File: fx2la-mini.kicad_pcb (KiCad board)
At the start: 4 copper layers, 21 x 13 mm, 26 parts, among them J1 USB_C_Receptacle_USB2.0, J2 Conn_02x05_Counter_Clockwise, U1 CY7C68013A-56LTX, U2 NUF8401MNT4G, U3 MIC5504-3.3YM5, U4 USBLC6-2SC6, Y1 24 MHz

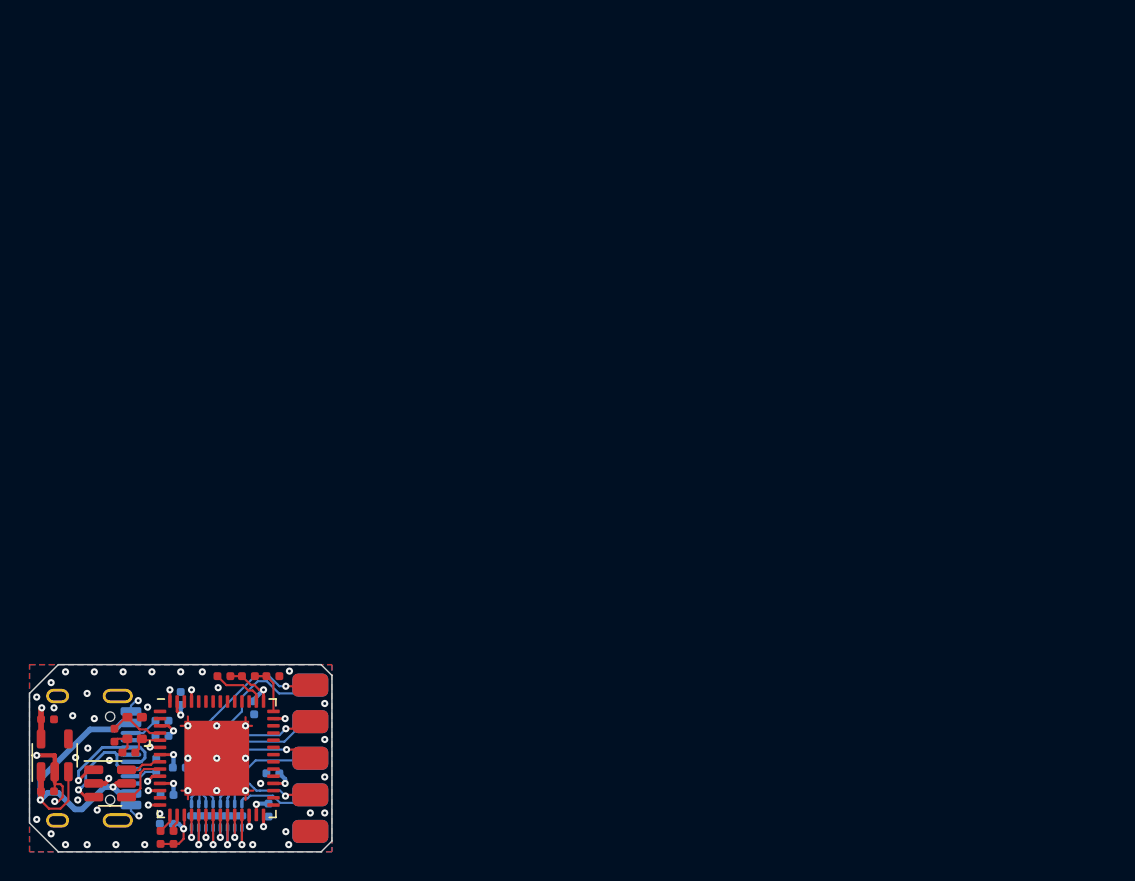
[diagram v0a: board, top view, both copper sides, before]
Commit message: Hijack project to 16 channels
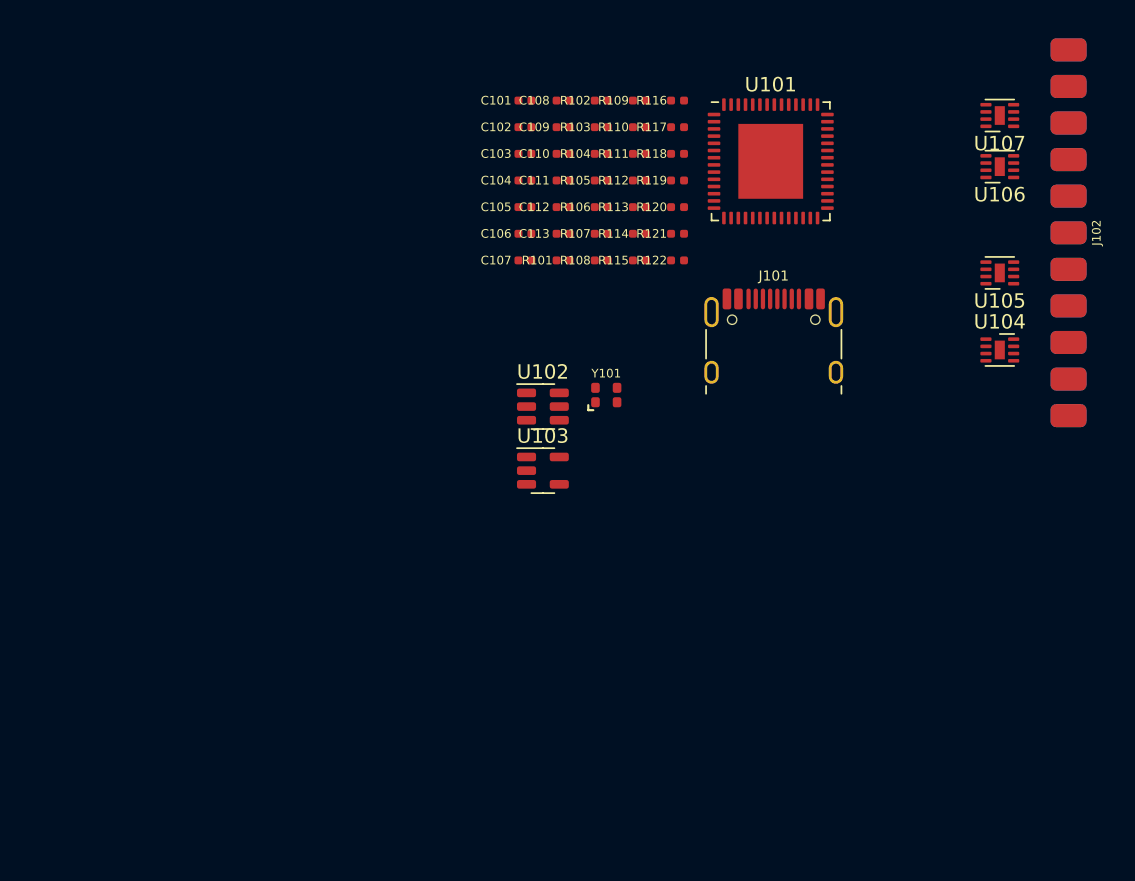
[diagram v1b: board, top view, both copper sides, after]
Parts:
- removed C1, C2: ~, passive:C_0402
- removed C10, C11, C12, C3, C4, C5, C6, C7, C9: 0.1u, passive:C_0402
- removed C13, C8: 4.7u, passive:C_0402
- removed J1: USB_C_Receptacle_USB2.0, connectors:USB_C_Receptacle_USB4105
- removed J2: Conn_02x05_Counter_Clockwise, connectors:2x5_2.54mm_side
- removed R1, R2, R3, R4, R5, R6: 5.1k, passive:R_0402
- removed U1: CY7C68013A-56LTX, Package_DFN_QFN:QFN-56-1EP_8x8mm_P0.5mm_EP4.5x5.2mm
- removed U2: NUF8401MNT4G, dfn:DFN-16-1EP_1.6x4mm_P0.5mm
- removed U3: MIC5504-3.3YM5, Package_TO_SOT_SMD:SOT-23-5
- removed U4: USBLC6-2SC6, Package_TO_SOT_SMD:SOT-23-6
- removed Y1: 24 MHz, crystals:Crystal_4Pin_2.0x1.6mm
- added C101: 16p, passive:C_0402, F.Cu at (146.4, 70.8)
- added C102: 16p, passive:C_0402, F.Cu at (146.4, 72.7)
- added C103: 100n, passive:C_0402, F.Cu at (146.4, 74.5)
- added C104: 100n, passive:C_0402, F.Cu at (146.4, 76.4)
- added C105: 100n, passive:C_0402, F.Cu at (146.4, 78.2)
- added C106: 100n, passive:C_0402, F.Cu at (146.4, 80.1)
- added C107: 100n, passive:C_0402, F.Cu at (146.4, 81.9)
- added C108: 4.7u, passive:C_0402, F.Cu at (149.1, 70.8)
- added C109: 100n, passive:C_0402, F.Cu at (149.1, 72.7)
- added C110: 100n, passive:C_0402, F.Cu at (149.1, 74.5)
- added C111: 100n, passive:C_0402, F.Cu at (149.1, 76.4)
- added C112: 100n, passive:C_0402, F.Cu at (149.1, 78.2)
- added C113: 4.7u, passive:C_0402, F.Cu at (149.1, 80.1)
- added J101: USB_C_Receptacle_USB2.0, connectors:USB_C_Receptacle_USB4105, F.Cu at (163.7, 88.0)
- added J102: Conn_02x11_Counter_Clockwise, connectors:2x11_2.54mm_side, F.Cu at (184.2, 80.0)
- added R101: 100k, passive:R_0402, F.Cu at (149.1, 81.9)
- added R102: 5.1k, passive:R_0402, F.Cu at (151.7, 70.8)
- added R103: 5.1k, passive:R_0402, F.Cu at (151.7, 72.7)
- added R104: 5.1k, passive:R_0402, F.Cu at (151.7, 74.5)
- added R105: 5.1k, passive:R_0402, F.Cu at (151.7, 76.4)
- added R106: 5.1k, passive:R_0402, F.Cu at (151.7, 78.2)
- added R107: 100k, passive:R_0402, F.Cu at (151.7, 80.1)
- added R108: 100k, passive:R_0402, F.Cu at (151.7, 81.9)
- added R109: 100k, passive:R_0402, F.Cu at (154.3, 70.8)
- added R110: 100k, passive:R_0402, F.Cu at (154.3, 72.7)
- added R111: 100k, passive:R_0402, F.Cu at (154.3, 74.5)
- added R112: 100k, passive:R_0402, F.Cu at (154.3, 76.4)
- added R113: 100k, passive:R_0402, F.Cu at (154.3, 78.2)
- added R114: 100k, passive:R_0402, F.Cu at (154.3, 80.1)
- added R115: 100k, passive:R_0402, F.Cu at (154.3, 81.9)
- added R116: 100k, passive:R_0402, F.Cu at (157.0, 70.8)
- added R117: 100k, passive:R_0402, F.Cu at (157.0, 72.7)
- added R118: 100k, passive:R_0402, F.Cu at (157.0, 74.5)
- added R119: 100k, passive:R_0402, F.Cu at (157.0, 76.4)
- added R120: 100k, passive:R_0402, F.Cu at (157.0, 78.2)
- added R121: 100k, passive:R_0402, F.Cu at (157.0, 80.1)
- added R122: 100k, passive:R_0402, F.Cu at (157.0, 81.9)
- added U101: CY7C68013A-56LTX, Package_DFN_QFN:QFN-56-1EP_8x8mm_P0.5mm_EP4.5x5.2mm, F.Cu at (163.5, 75.0)
- added U102: USBLC6-2SC6, Package_TO_SOT_SMD:SOT-23-6, F.Cu at (147.7, 92.1)
- added U103: MIC5235-3.3YM5-TR, Package_TO_SOT_SMD:SOT-23-5, F.Cu at (147.7, 96.5)
- added U104: NUF4401MN, Package_DFN_QFN:DFN-8-1EP_2x2mm_P0.5mm_EP0.7x1.3mm, F.Cu at (179.4, 88.2)
- added U105: NUF4401MN, Package_DFN_QFN:DFN-8-1EP_2x2mm_P0.5mm_EP0.7x1.3mm, F.Cu at (179.4, 82.8)
- added U106: NUF4401MN, Package_DFN_QFN:DFN-8-1EP_2x2mm_P0.5mm_EP0.7x1.3mm, F.Cu at (179.4, 75.4)
- added U107: NUF4401MN, Package_DFN_QFN:DFN-8-1EP_2x2mm_P0.5mm_EP0.7x1.3mm, F.Cu at (179.4, 71.9)
- added Y101: 24 MHz, crystals:Crystal_4Pin_2.0x1.6mm, F.Cu at (152.1, 91.3)
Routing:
- net +3V3: track 60.1 -> 0.00 mm, vias 9 -> 0
- net +5V: track 24.6 -> 0.00 mm, vias 2 -> 0
- net GND: track 23.1 -> 0.00 mm, vias 59 -> 0
- net /PB0_OUT: track 14.9 -> 0.00 mm, vias 1 -> 0
- net /PB1_OUT: track 14.5 -> 0.00 mm
- net /PB2_OUT: track 11.6 -> 0.00 mm, vias 1 -> 0
- net /PB3_OUT: track 10.8 -> 0.00 mm
- net /PB4_OUT: track 9.39 -> 0.00 mm, vias 1 -> 0
- net /D_P: track 8.95 -> 0.00 mm, vias 1 -> 0
- net /D_N: track 8.37 -> 0.00 mm, vias 1 -> 0
- net /PB5_OUT: track 7.69 -> 0.00 mm
- net /PB6_OUT: track 6.76 -> 0.00 mm, vias 1 -> 0
- net /PB7_OUT: track 5.59 -> 0.00 mm
- net /XIN: track 3.95 -> 0.00 mm
- net /DP_N: track 3.76 -> 0.00 mm
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- removed copper zone on B.Cu, net GND
- removed copper zone on F.Cu, net GND
- removed copper zone on In1.Cu, net GND
- removed copper zone on In2.Cu, net GND
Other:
- board outline removed

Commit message: Layout complete
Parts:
- moved R110 35.7 mm to (184.7, 91.4)
- moved R108 33.7 mm to (182.6, 68.5), turned to 180 degrees
- moved C108 32.9 mm to (176.6, 88.9)
- moved C104 32.3 mm to (178.7, 75.3), turned to -90 degrees
- moved R114 31.6 mm to (184.7, 88.9)
- moved U103 31.3 mm to (177.2, 86.3), turned to 90 degrees
- moved R107 31.1 mm to (182.6, 83.8), turned to 180 degrees
- moved R109 30.8 mm to (184.7, 76.2)
- moved R113 30.7 mm to (184.7, 73.7)
- moved R111 30.6 mm to (182.6, 86.3), turned to 180 degrees
- moved C110 30.3 mm to (178.7, 68.2), turned to 90 degrees
- moved R118 30.1 mm to (184.7, 86.3)
- moved R121 30.0 mm to (184.7, 68.5)
- moved R119 29.7 mm to (182.6, 91.4), turned to 180 degrees
- moved U102 29.4 mm to (174.4, 79.8), turned to 90 degrees
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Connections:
- R107 pad 1: /CH3 -> /CH3_OUT
- R108 pad 1: /CH7 -> /CH7_OUT
- R109 pad 1: /CH11 -> /CH11_OUT
- R110 pad 1: /CH15 -> /CH15_OUT
- R111 pad 1: /CH2 -> /CH2_OUT
- R112 pad 1: /CH6 -> /CH6_OUT
- R113 pad 1: /CH10 -> /CH10_OUT
- R114 pad 1: /CH14 -> /CH14_OUT
- R115 pad 1: /CH1 -> /CH1_OUT
- R116 pad 1: /CH5 -> /CH5_OUT
- R117 pad 1: /CH9 -> /CH9_OUT
- R118 pad 1: /CH13 -> /CH13_OUT
- R119 pad 1: /CH0 -> /CH0_OUT
- R120 pad 1: /CH4 -> /CH4_OUT
- R121 pad 1: /CH8 -> /CH8_OUT
- R122 pad 1: /CH12 -> /CH12_OUT
- U102 pad 1: /D_N -> /D_P
- U102 pad 3: /D_P -> /D_N
- U102 pad 4: /DP_P -> /DP_N
- U102 pad 6: /DP_N -> /DP_P
- U104 pad 1: /CH0 -> /CH3
- U104 pad 2: /CH1 -> /CH2
- U104 pad 3: /CH2 -> /CH1
- U104 pad 4: /CH3 -> /CH0
- U104 pad 5: /CH3_OUT -> /CH0_OUT
- U104 pad 6: /CH2_OUT -> /CH1_OUT
- U104 pad 7: /CH1_OUT -> /CH2_OUT
- U104 pad 8: /CH0_OUT -> /CH3_OUT
- U105 pad 1: /CH4 -> /CH7
- U105 pad 2: /CH5 -> /CH6
- U105 pad 3: /CH6 -> /CH5
- U105 pad 4: /CH7 -> /CH4
- U105 pad 5: /CH7_OUT -> /CH4_OUT
- U105 pad 6: /CH6_OUT -> /CH5_OUT
- U105 pad 7: /CH5_OUT -> /CH6_OUT
- U105 pad 8: /CH4_OUT -> /CH7_OUT
- U106 pad 1: /CH8 -> /CH11
- U106 pad 2: /CH9 -> /CH10
- U106 pad 3: /CH10 -> /CH9
- U106 pad 4: /CH11 -> /CH8
- U106 pad 5: /CH11_OUT -> /CH8_OUT
- U106 pad 6: /CH10_OUT -> /CH9_OUT
- U106 pad 7: /CH9_OUT -> /CH10_OUT
- U106 pad 8: /CH8_OUT -> /CH11_OUT
- U107 pad 1: /CH12 -> /CH15
- U107 pad 2: /CH13 -> /CH14
- U107 pad 3: /CH14 -> /CH13
- U107 pad 4: /CH15 -> /CH12
- U107 pad 5: /CH15_OUT -> /CH12_OUT
- U107 pad 6: /CH14_OUT -> /CH13_OUT
- U107 pad 7: /CH13_OUT -> /CH14_OUT
- U107 pad 8: /CH12_OUT -> /CH15_OUT
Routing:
- net +3V3: track 0.00 -> 63.0 mm, vias 0 -> 10
- net /CH15_OUT: track 0.00 -> 28.4 mm, vias 0 -> 2
- net /CH14_OUT: track 0.00 -> 27.0 mm, vias 0 -> 2
- net /CH13_OUT: track 0.00 -> 26.3 mm, vias 0 -> 2
- net /CH12_OUT: track 0.00 -> 24.9 mm, vias 0 -> 2
- net +5V: track 0.00 -> 24.3 mm, vias 0 -> 3
- net /CH11_OUT: track 0.00 -> 23.8 mm, vias 0 -> 2
- net /CH10_OUT: track 0.00 -> 23.5 mm, vias 0 -> 2
- net /CH9_OUT: track 0.00 -> 22.8 mm, vias 0 -> 2
- net /CH8_OUT: track 0.00 -> 21.2 mm, vias 0 -> 2
- net /CH0_OUT: track 0.00 -> 16.5 mm
- net /CH1_OUT: track 0.00 -> 13.7 mm
- net /CH2_OUT: track 0.00 -> 11.0 mm
- net /D_N: track 0.00 -> 10.0 mm, vias 0 -> 2
- net /D_P: track 0.00 -> 10.00 mm
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- added copper zone on B.Cu, net GND
- added copper zone on F.Cu, net GND
- added copper zone on In1.Cu, net GND
- added copper zone on In2.Cu, net GND
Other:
- board outline added: 21.5 x 28 mm
- board text added: "0"
- board text added: "1"
- board text added: "10"
- board text added: "11"
- board text added: "12"
- board text added: "13"
- board text added: "14"
- board text added: "15"
- board text added: "16ch FX2LA"
- board text added: "2"
- board text added: "3"
- board text added: "4"
- board text added: "5"
- board text added: "6"
- board text added: "7"
- board text added: "8"
- board text added: "9"
- board text added: "@korken89"
- board text added: "Emil Fresk"
- board text added: "G"

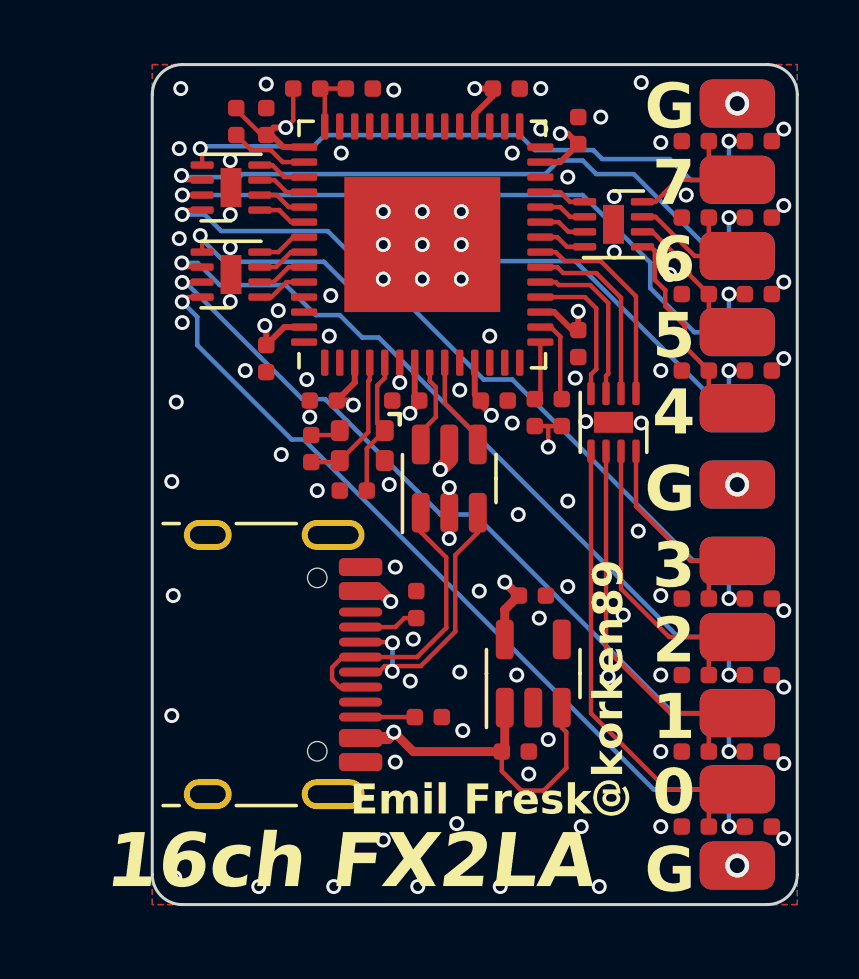
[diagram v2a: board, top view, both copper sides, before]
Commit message: Add LED to PA1, update some part numbers that were out of stock now
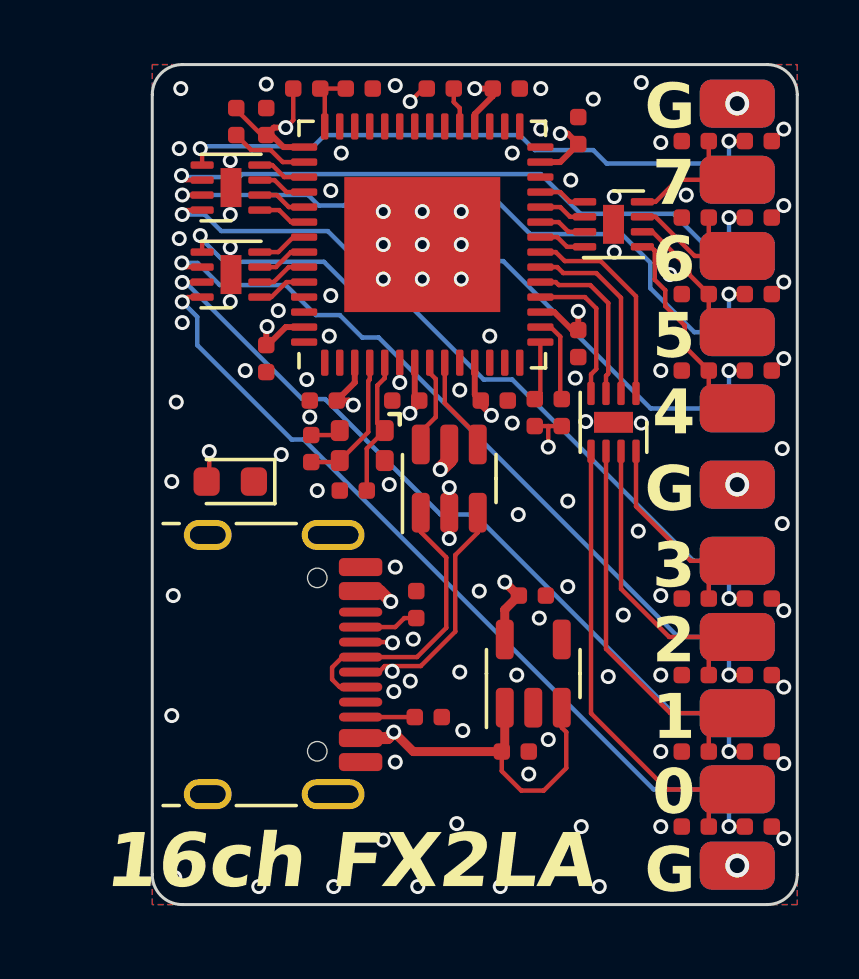
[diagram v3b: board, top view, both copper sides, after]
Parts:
- added D101: LED_Small, LED_SMD:LED_0603_1608Metric, F.Cu at (167.1, 79.9)
- added R123: 330, passive:R_0402, F.Cu at (174.1, 66.8)
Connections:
- U101 pad 33: unconnected-(U101-PA0/~{INT0}-Pad33) -> /LED
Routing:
- net Net-(D101-A): track 0.00 -> 18.9 mm, vias 0 -> 2
- net /LED: track 0.00 -> 1.35 mm
- net GND: vias 95 -> 99
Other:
- board text added: "Emil Fresk @korken89"
- board text added: "v1.0"
- board text removed: "@korken89"
- board text removed: "Emil Fresk"
